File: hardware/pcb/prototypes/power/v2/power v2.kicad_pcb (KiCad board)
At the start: 2 copper layers, 15.2 x 71.1 mm, 48 parts, among them J1 5V OUT, J2 USB_PD, J3 D_PIN, J4 USB_C_Receptacle_USB2.0_16P, J5 D_PIN, U1 TPS25730AD, U2 TUSB321, U3 TPS2116DRL

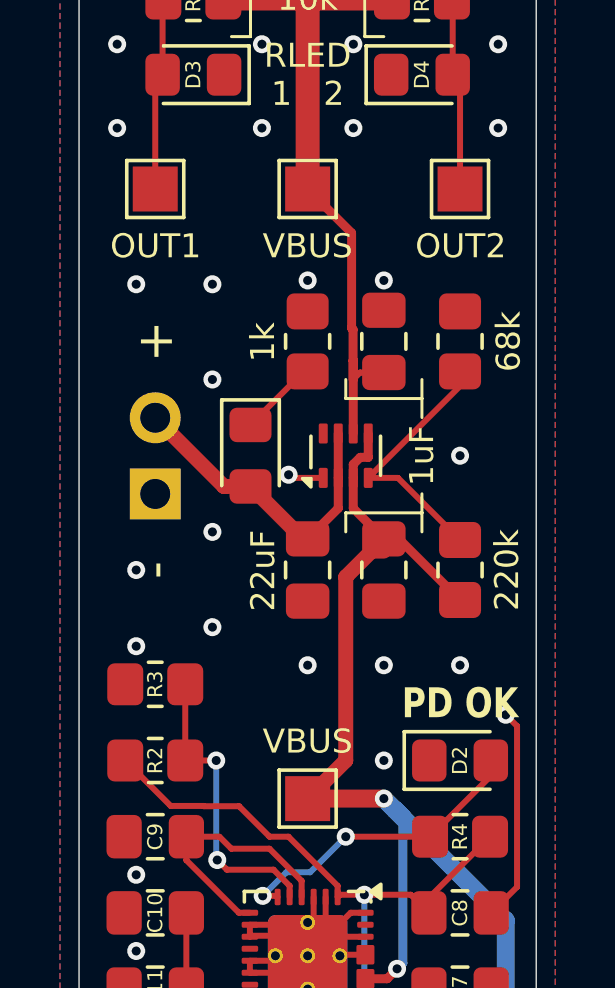
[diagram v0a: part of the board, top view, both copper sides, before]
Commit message: separate gnd and 5V
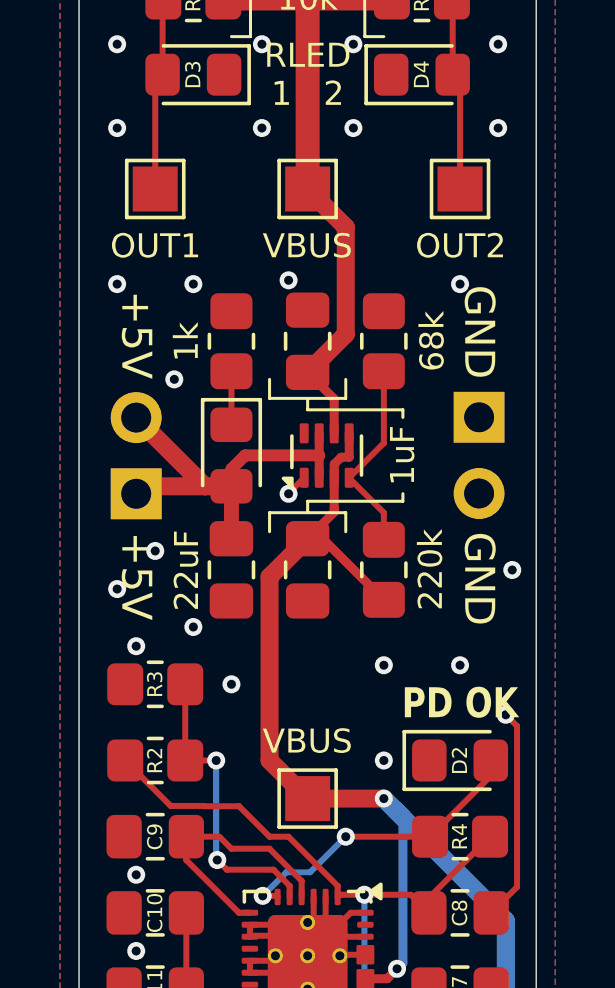
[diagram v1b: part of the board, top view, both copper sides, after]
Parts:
- added J6: GND, Connector_PinHeader_2.54mm:PinHeader_1x02_P2.54mm_Vertical, F.Cu at (95.9, 73.7)
- moved C22 2.54 mm to (87.6, 78.7)
- moved R1 2.54 mm to (87.6, 71.1)
- moved R10 2.54 mm to (92.7, 71.1)
- moved R9 2.54 mm to (92.7, 78.7)
- moved C20 2.54 mm to (90.2, 78.7)
- moved C21 2.54 mm to (90.2, 71.1)
- moved D1 0.64 mm to (87.6, 74.9)
- moved J1 0.64 mm to (84.5, 76.2)
- moved U3 0.64 mm to (90.8, 74.9)
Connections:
- J1 pad 1: GND -> +5V
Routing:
- net +5V: track 10.7 -> 13.4 mm
- net /Input Selector/PR1: track 8.73 -> 6.58 mm
- net /5V USB/VBUS_USB: track 58.2 -> 57.2 mm
- net Net-(D1-K): track 2.64 -> 1.79 mm
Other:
- board text added: "+5V"
- board text added: "GND"
- board text removed: "+"
- board text removed: "-"
